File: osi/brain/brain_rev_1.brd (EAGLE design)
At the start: 25.4 x 25.4 mm, 8 parts, among them IC1 TINY24/44/84-PU

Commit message: chuck
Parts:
- added R2, R3: (no value), adafruit_mod:0204V
- moved JP8 1.27 mm to (6.35, 24.1)
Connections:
- net +3V3: now also R2.1, R3.1
- net SCL_D4: now also R3.2
- net SDA_D6: now also R2.2
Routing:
- net +3V3: track 39.4 -> 50.0 mm
- net SDA_D6: track 37.0 -> 42.6 mm
- net SCL_D4: track 34.8 -> 39.1 mm
- net D2: track 16.8 -> 17.9 mm
- net D3: track 11.9 -> 13.0 mm
- net D7: track 14.1 -> 13.3 mm

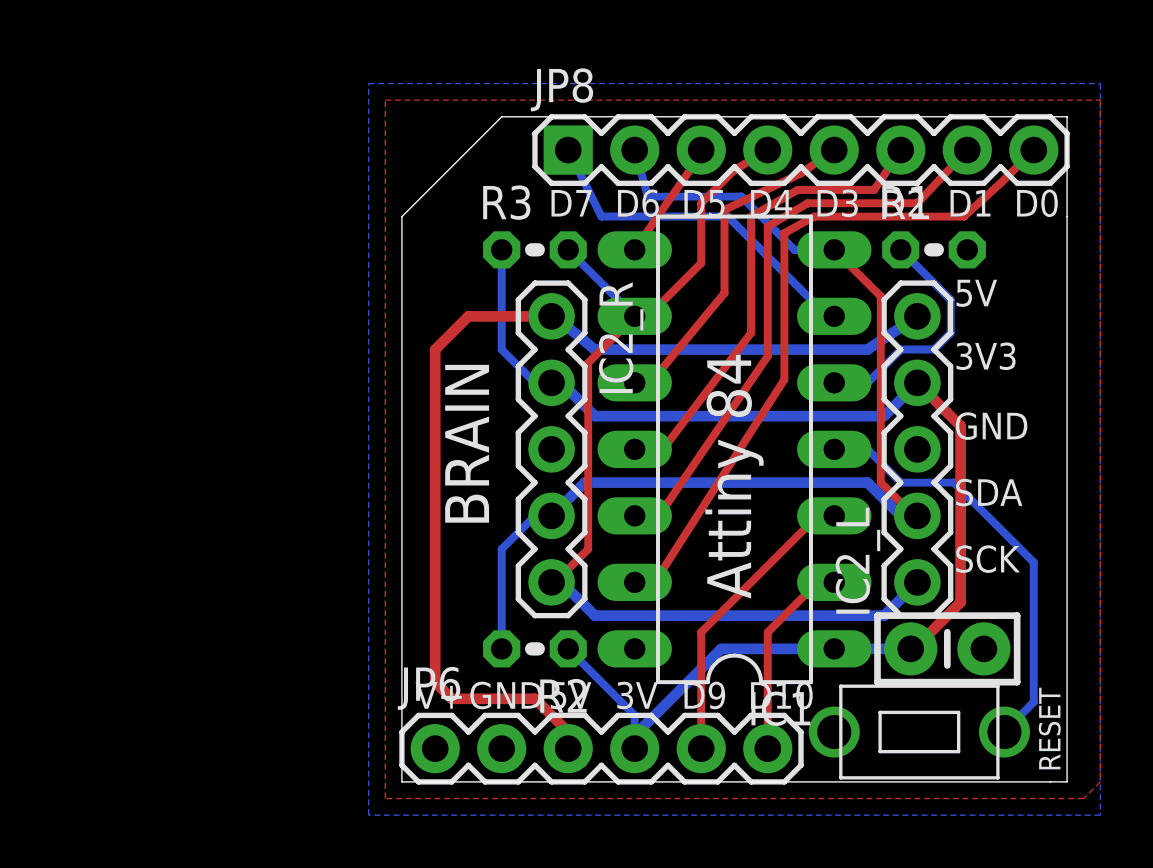
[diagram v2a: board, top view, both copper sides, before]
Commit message: D9 -> D8 for INT0
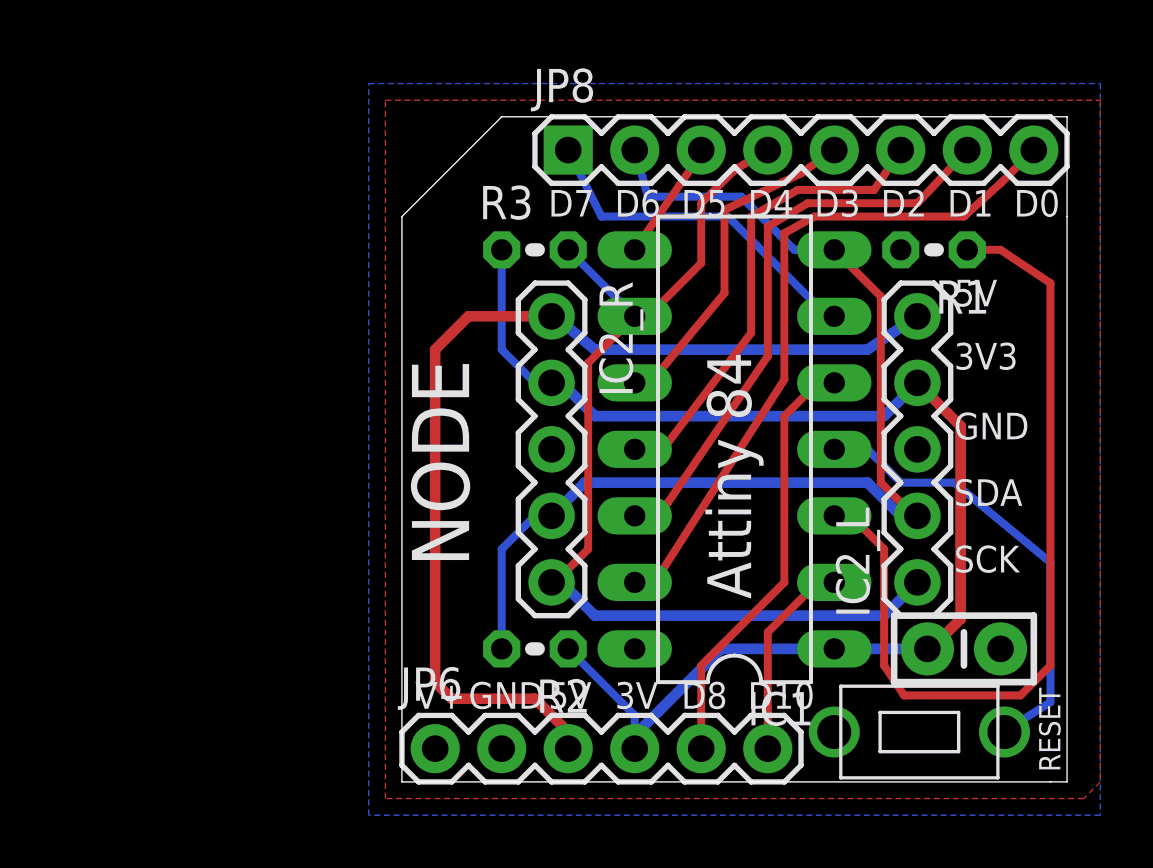
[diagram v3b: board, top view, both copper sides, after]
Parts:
- moved C1 0.64 mm to (21.5, 5.08)
- turned R1 to 180 degrees
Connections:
- net D8: now also JP6.5; no longer R1.1
- net D9: now also R1.1; no longer JP6.5
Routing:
- net D9: track 11.4 -> 32.5 mm
- net D8: track 9.20 -> 16.4 mm
- net RESET: track 16.3 -> 17.3 mm
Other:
- board text added: "D8"
- board text added: "NODE"
- board text added: "Rev 1 Mar 12"
- board text removed: "BRAIN"
- board text removed: "Brain Rev 1 Feb 12"
- board text removed: "D9"
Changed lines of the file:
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@@
 <setting verticaltext="up"/>
 </settings>
-<grid distance="0.05" unitdist="inch" unit="inch" style="lines" multiple="1" display="yes" altdistance="0.005" altunitdist="inch" altunit="inch"/>
+<grid distance="0.025" unitdist="inch" unit="inch" style="lines" multiple="1" display="yes" altdistance="0.005" altunitdist="inch" altunit="inch"/>
 <layers>
 <layer number="1" name="Top" color="4" fill="1" visible="yes" active="yes"/>
@@
 <layer number="20" name="Dimension" color="15" fill="1" visible="yes" active="yes"/>
 <layer number="21" name="tPlace" color="16" fill="1" visible="yes" active="yes"/>
-<layer number="22" name="bPlace" color="14" fill="1" visible="yes" active="yes"/>
+<layer number="22" name="bPlace" color="14" fill="1" visible="no" active="yes"/>
 <layer number="23" name="tOrigins" color="15" fill="1" visible="yes" active="yes"/>
 <layer number="24" name="bOrigins" color="15" fill="1" visible="yes" active="yes"/>
@@
 <text x="25.146" y="0.381" size="0.8128" layer="21" font="vector" ratio="15" rot="R90">RESET</text>
 <text x="13.335" y="6.985" size="1.6764" layer="21" font="vector" ratio="10" rot="R90">Attiny 84</text>
-<text x="1.651" y="16.129" size="1.6764" layer="21" font="vector" ratio="20" rot="R270">BRAIN</text>
+<text x="0.381" y="16.129" size="2.1844" layer="21" font="vector" ratio="20" rot="R270">NODE</text>
 <text x="0.635" y="4.953" size="0.8128" layer="22" font="vector" ratio="15" rot="MR90">MakersBox.blogspot.com</text>
 <text x="23.622" y="3.683" size="1.27" layer="22" font="vector" ratio="15" rot="MR90">One Square Inch</text>
-<text x="10.668" y="14.859" size="1.016" layer="22" font="vector" ratio="12" rot="MR90">Brain
-Rev 1
-Feb 12</text>
+<text x="10.668" y="13.589" size="1.4224" layer="22" font="vector" ratio="12" rot="MR90">Rev 1
+Mar 12</text>
 <text x="21.082" y="15.748" size="1.016" layer="21" font="vector" ratio="10">3V3</text>
 <text x="21.082" y="13.081" size="1.016" layer="21" font="vector" ratio="10">GND</text>
@@
 <text x="5.588" y="2.794" size="1.016" layer="21" font="vector" ratio="15">5V</text>
 <text x="8.128" y="2.794" size="1.016" layer="21" font="vector" ratio="15">3V</text>
-<text x="10.668" y="2.794" size="1.016" layer="21" font="vector" ratio="15">D9</text>
+<text x="10.668" y="2.794" size="1.016" layer="21" font="vector" ratio="15">D8</text>
 <text x="13.208" y="2.794" size="1.016" layer="21" font="vector" ratio="15">D10</text>
 <text x="2.032" y="2.794" size="1.016" layer="22" font="vector" ratio="15" rot="MR0">V+</text>
@@
 <text x="7.112" y="2.794" size="1.016" layer="22" font="vector" ratio="15" rot="MR0">5V</text>
 <text x="9.652" y="2.794" size="1.016" layer="22" font="vector" ratio="15" rot="MR0">3V</text>
-<text x="12.192" y="2.794" size="1.016" layer="22" font="vector" ratio="15" rot="MR0">D9</text>
+<text x="12.192" y="2.794" size="1.016" layer="22" font="vector" ratio="15" rot="MR0">D8</text>
 <text x="15.494" y="2.794" size="1.016" layer="22" font="vector" ratio="15" rot="MR0">D10</text>
 <text x="7.112" y="21.59" size="1.016" layer="22" font="vector" ratio="15" rot="MR0">D7</text>
@@
 <text x="22.352" y="21.59" size="1.016" layer="22" font="vector" ratio="15" rot="MR0">D1</text>
 <text x="24.892" y="21.59" size="1.016" layer="22" font="vector" ratio="15" rot="MR0">D0</text>
+<text x="12.065" y="4.445" size="2.1844" layer="22" ratio="12" rot="SMR90">NODE</text>
 </plain>
 <attributes>
@@
 <elements>
 <element name="IC1" library="avr-7" package="DIL14" value="TINY24/44/84-PU" x="12.7" y="12.7" rot="R90"/>
-<element name="C1" library="SparkFun" package="CAP-PTH-SMALL-KIT" value="" x="20.828" y="5.08" rot="R180"/>
+<element name="C1" library="SparkFun" package="CAP-PTH-SMALL-KIT" value="" x="21.463" y="5.08" rot="R180"/>
 <element name="U$1" library="_my-parts" package="PTS635_SWITCH" value="PTS635_SWITCH" x="16.51" y="1.905"/>
 <element name="IC2_L" library="SparkFun_mod" package="1X05" value="" x="19.685" y="7.62" rot="R90"/>
@@
 <element name="JP6" library="SparkFun" package="1X06" value="" x="1.27" y="1.27"/>
 <element name="JP8" library="SparkFun" package="1X08" value="" x="6.35" y="24.13"/>
-<element name="R1" library="adafruit_mod" package="0204V" value="" x="20.32" y="20.32"/>
+<element name="R1" library="adafruit_mod" package="0204V" value="" x="20.32" y="20.32" rot="R180"/>
 <element name="R2" library="adafruit_mod" package="0204V" value="" x="5.08" y="5.08" rot="R180"/>
 <element name="R3" library="adafruit_mod" package="0204V" value="" x="5.08" y="20.32"/>
@@
 <wire x1="17.78" y1="12.7" x2="19.05" y2="11.43" width="0.3048" layer="16"/>
 <wire x1="19.05" y1="11.43" x2="21.082" y2="11.43" width="0.3048" layer="16"/>
-<wire x1="21.082" y1="11.43" x2="24.13" y2="8.382" width="0.3048" layer="16"/>
-<wire x1="24.13" y1="8.382" x2="24.13" y2="3.048" width="0.3048" layer="16"/>
-<wire x1="24.13" y1="3.048" x2="23.01" y2="1.928" width="0.3048" layer="16"/>
+<wire x1="21.082" y1="11.43" x2="24.765" y2="8.382" width="0.3048" layer="16"/>
+<wire x1="24.765" y1="8.382" x2="24.765" y2="3.048" width="0.3048" layer="16"/>
+<wire x1="24.765" y1="3.048" x2="23.01" y2="1.928" width="0.3048" layer="16"/>
 <wire x1="23.01" y1="1.928" x2="23.01" y2="1.905" width="0.3048" layer="16"/>
 </signal>
@@
 <signal name="D9">
 <contactref element="IC1" pad="3"/>
-<contactref element="JP6" pad="5"/>
-<wire x1="16.51" y1="10.16" x2="15.875" y2="10.16" width="0.3048" layer="1"/>
-<wire x1="15.875" y1="10.16" x2="11.43" y2="5.715" width="0.3048" layer="1"/>
-<wire x1="11.43" y1="5.715" x2="11.43" y2="1.27" width="0.3048" layer="1"/>
+<contactref element="R1" pad="1"/>
+<wire x1="16.51" y1="10.16" x2="17.145" y2="10.16" width="0.3048" layer="1"/>
+<wire x1="17.145" y1="10.16" x2="18.415" y2="8.89" width="0.3048" layer="1"/>
+<wire x1="18.415" y1="8.89" x2="18.415" y2="4.445" width="0.3048" layer="1"/>
+<wire x1="18.415" y1="4.445" x2="19.177" y2="3.302" width="0.3048" layer="1"/>
+<wire x1="19.177" y1="3.302" x2="23.622" y2="3.302" width="0.3048" layer="1"/>
+<wire x1="23.622" y1="3.302" x2="24.765" y2="4.445" width="0.3048" layer="1"/>
+<wire x1="24.765" y1="4.445" x2="24.765" y2="19.05" width="0.3048" layer="1"/>
+<wire x1="24.765" y1="19.05" x2="22.86" y2="20.32" width="0.3048" layer="1"/>
+<wire x1="22.86" y1="20.32" x2="21.59" y2="20.32" width="0.3048" layer="1"/>
 </signal>
 <signal name="D10">
@@
 <contactref element="IC1" pad="1"/>
 <contactref element="C1" pad="2"/>
-<wire x1="19.431" y1="5.08" x2="19.685" y2="5.08" width="0.4064" layer="16"/>
+<wire x1="20.066" y1="5.08" x2="19.685" y2="5.08" width="0.4064" layer="16"/>
 <contactref element="JP6" pad="4"/>
 <wire x1="19.685" y1="15.24" x2="18.415" y2="13.97" width="0.4064" layer="16"/>
@@
 <wire x1="12.192" y1="5.08" x2="8.89" y2="1.778" width="0.4064" layer="16"/>
 <wire x1="8.89" y1="1.778" x2="8.89" y2="1.27" width="0.4064" layer="16"/>
-<wire x1="19.431" y1="5.08" x2="16.51" y2="5.08" width="0.4064" layer="16"/>
+<wire x1="20.066" y1="5.08" x2="16.51" y2="5.08" width="0.4064" layer="16"/>
 <wire x1="19.685" y1="15.24" x2="21.336" y2="13.589" width="0.4064" layer="1"/>
-<wire x1="21.336" y1="13.589" x2="21.336" y2="6.858" width="0.4064" layer="1"/>
-<wire x1="21.336" y1="6.858" x2="19.558" y2="5.08" width="0.4064" layer="1"/>
-<wire x1="19.558" y1="5.08" x2="19.431" y2="5.08" width="0.4064" layer="1"/>
+<wire x1="21.336" y1="13.589" x2="21.336" y2="6.223" width="0.4064" layer="1"/>
+<wire x1="21.336" y1="6.223" x2="20.193" y2="5.08" width="0.4064" layer="1"/>
+<wire x1="20.193" y1="5.08" x2="20.066" y2="5.08" width="0.4064" layer="1"/>
 <contactref element="R3" pad="1"/>
 <contactref element="R2" pad="1"/>
@@
 <signal name="D8">
 <contactref element="IC1" pad="5"/>
-<contactref element="R1" pad="1"/>
-<wire x1="16.51" y1="15.24" x2="17.78" y2="15.24" width="0.3048" layer="16"/>
-<wire x1="17.78" y1="15.24" x2="19.05" y2="16.51" width="0.3048" layer="16"/>
-<wire x1="19.05" y1="16.51" x2="20.32" y2="16.51" width="0.3048" layer="16"/>
-<wire x1="20.32" y1="16.51" x2="20.955" y2="17.145" width="0.3048" layer="16"/>
-<wire x1="20.955" y1="17.145" x2="20.955" y2="18.415" width="0.3048" layer="16"/>
-<wire x1="20.955" y1="18.415" x2="19.05" y2="20.32" width="0.3048" layer="16"/>
+<contactref element="JP6" pad="5"/>
+<wire x1="16.51" y1="15.24" x2="15.875" y2="15.24" width="0.3048" layer="1"/>
+<wire x1="15.875" y1="15.24" x2="14.605" y2="13.97" width="0.3048" layer="1"/>
+<wire x1="14.605" y1="13.97" x2="14.605" y2="7.62" width="0.3048" layer="1"/>
+<wire x1="14.605" y1="7.62" x2="11.43" y2="4.445" width="0.3048" layer="1"/>
+<wire x1="11.43" y1="4.445" x2="11.43" y2="1.27" width="0.3048" layer="1"/>
 </signal>
 </signals>

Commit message: FURBY
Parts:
- added U$2: 2.1MMJACKTHM, adafruit:PJ-102A
- moved R1 1.91 mm to (20.3, 22.2)
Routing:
- net +3V3: track 50.5 -> 0.00 mm
- net SDA_D6: track 42.6 -> 0.00 mm
- net SCL_D4: track 39.1 -> 0.00 mm
- net +5V: track 39.0 -> 0.00 mm
- net D9: track 32.5 -> 0.00 mm
- net AREF_D0: track 26.3 -> 0.00 mm
- net D1: track 21.9 -> 0.00 mm
- net D2: track 17.9 -> 0.00 mm
- net RESET: track 17.3 -> 0.00 mm
- net D8: track 16.4 -> 0.00 mm
- net D7: track 13.3 -> 0.00 mm
- net D3: track 13.0 -> 0.00 mm
- net D10: track 7.77 -> 0.00 mm
- net D5: track 4.58 -> 0.00 mm
